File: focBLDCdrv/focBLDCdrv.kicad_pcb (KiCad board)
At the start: 2 copper layers, 78.5 x 50 mm, 19 parts, among them J1 Screw_Terminal_01x02, J2 Screw_Terminal_01x03, J5 Conn_02x03_Counter_Clockwise, J6 Conn_01x03, U1 MFC8316A

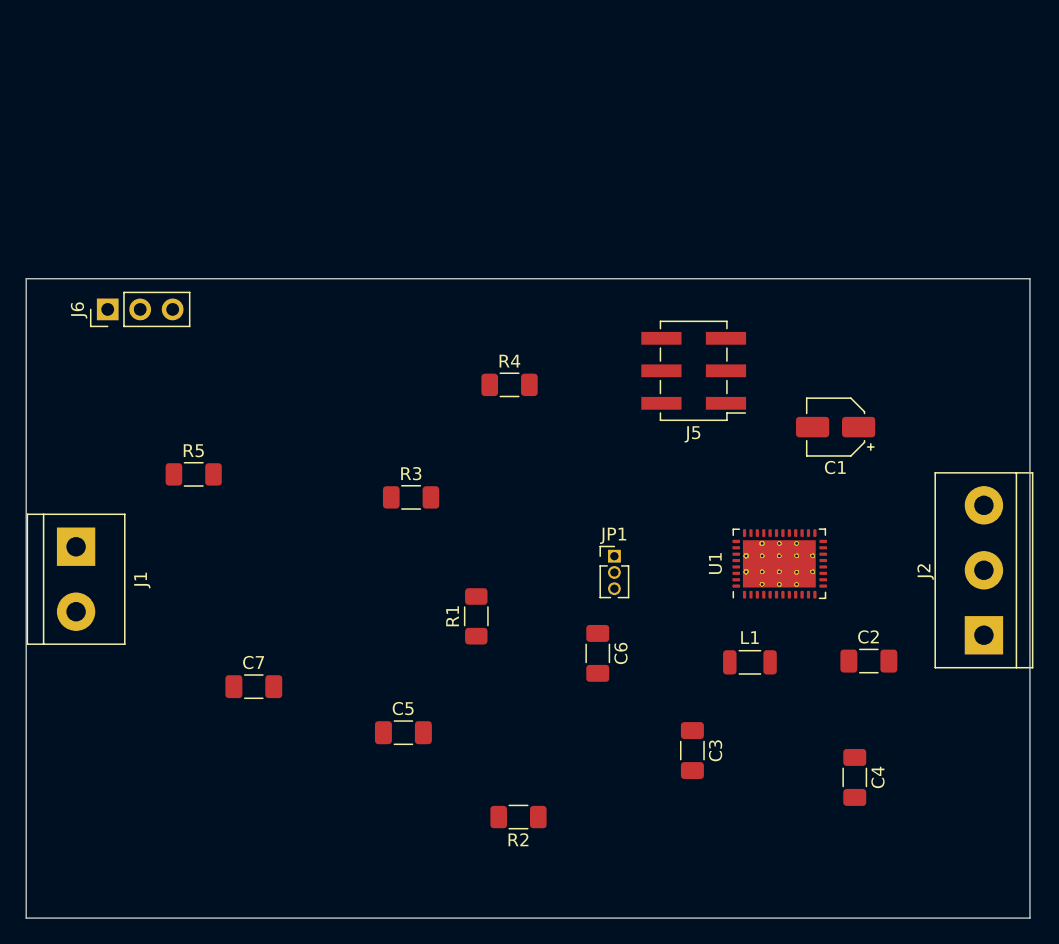
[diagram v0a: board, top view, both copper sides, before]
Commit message: J4 header orientation changed, mount holes added and additinal AGND fill
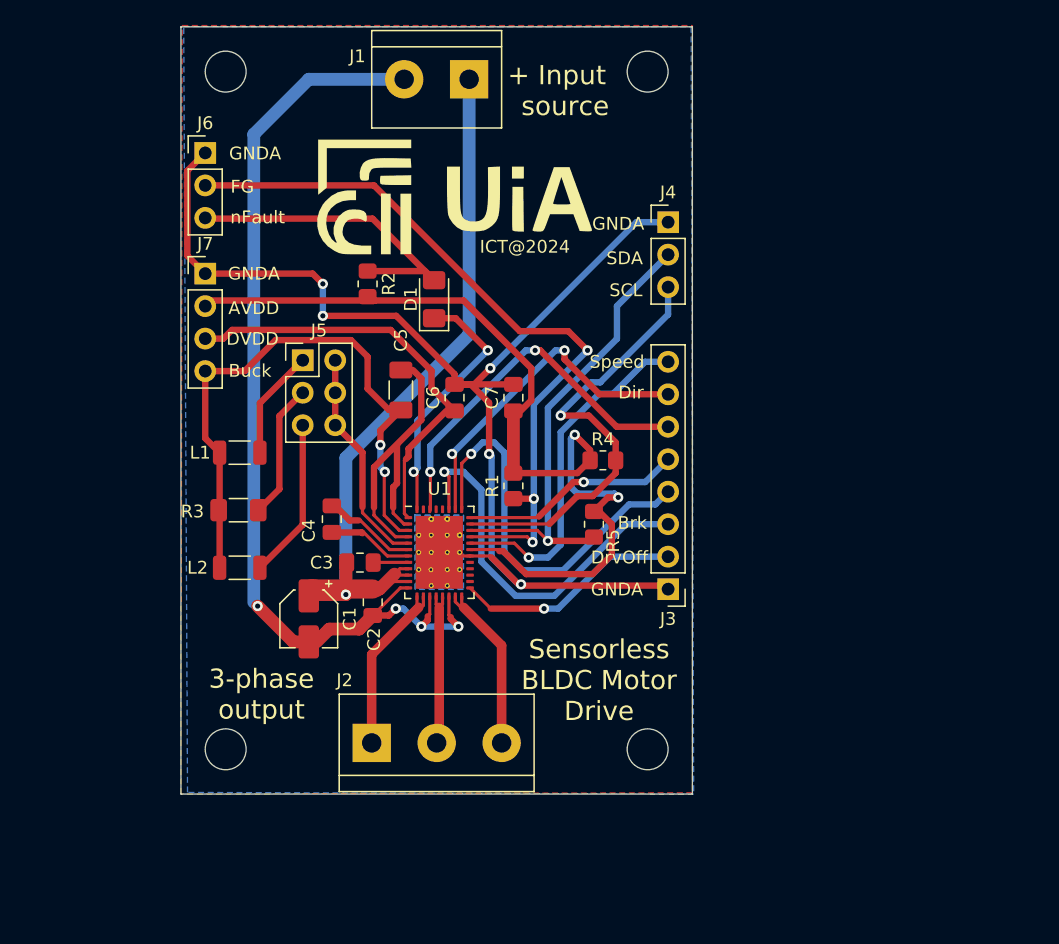
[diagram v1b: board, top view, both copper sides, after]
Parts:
- removed JP1: Jumper_3_Open, Connector_PinHeader_1.27mm:PinHeader_1x03_P1.27mm_Vertical
- added D1: LED, LED_SMD:LED_1206_3216Metric_Pad1.42x1.75mm_HandSolder, F.Cu at (147.9, 88.0)
- added G***: LOGO, UiA-Logo:uiaLogo, F.Cu at (149.5, 80.0)
- added J3: Conn_01x08, Connector_PinHeader_2.54mm:PinHeader_1x08_P2.54mm_Vertical, F.Cu at (166.2, 110.7)
- added J4: i2c, Connector_PinHeader_2.54mm:PinHeader_1x03_P2.54mm_Vertical, F.Cu at (166.2, 82.0)
- added J7: Power Out, Connector_PinHeader_2.54mm:PinHeader_1x04_P2.54mm_Vertical, F.Cu at (130.0, 86.0)
- added L2: 22µ, Inductor_SMD:L_1206_3216Metric, F.Cu at (132.7, 109.0)
- added REF**: MountingHole_3.2mm_M3, MountingHole:MountingHole_3.2mm_M3, F.Cu at (131.6, 70.2)
- added REF**: MountingHole_3.2mm_M3, MountingHole:MountingHole_3.2mm_M3, F.Cu at (164.6, 70.2)
- added REF**: MountingHole_3.2mm_M3, MountingHole:MountingHole_3.2mm_M3, F.Cu at (131.6, 123.2)
- added REF**: MountingHole_3.2mm_M3, MountingHole:MountingHole_3.2mm_M3, F.Cu at (164.6, 123.2)
- C2, C3, C4, C6, C7: footprint Capacitor_SMD:C_1206_3216Metric_Pad1.33x1.80mm_HandSolder -> Capacitor_SMD:C_0805_2012Metric_Pad1.18x1.45mm_HandSolder
- J5: value Conn_02x03_Counter_Clockwise -> Conn_02x03_Top_Bottom; footprint Connector_PinHeader_2.54mm:PinHeader_2x03_P2.54mm_Vertical_SMD -> Connector_PinHeader_2.54mm:PinHeader_2x03_P2.54mm_Vertical
- J6: value Conn_01x03 -> Monitor port
- R1: value 22 -> 4.7k; footprint Resistor_SMD:R_1206_3216Metric_Pad1.30x1.75mm_HandSolder -> Resistor_SMD:R_0805_2012Metric_Pad1.20x1.40mm_HandSolder
- R2: value 5.1k -> 1k; footprint Resistor_SMD:R_1206_3216Metric_Pad1.30x1.75mm_HandSolder -> Resistor_SMD:R_0805_2012Metric_Pad1.20x1.40mm_HandSolder
- R3: value 5.1k -> 22
- R4, R5: value 5.1k -> 4.7k; footprint Resistor_SMD:R_1206_3216Metric_Pad1.30x1.75mm_HandSolder -> Resistor_SMD:R_0805_2012Metric_Pad1.20x1.40mm_HandSolder
- moved J2 48.6 mm to (143.0, 122.7), turned to 0 degrees
- moved J1 47.8 mm to (150.6, 70.8), turned to 180 degrees
- moved C4 45.6 mm to (139.9, 105.2), turned to 90 degrees
- moved C1 43.8 mm to (138.1, 113.0), turned to -90 degrees
- moved R2 43.3 mm to (142.7, 86.8), turned to -90 degrees
- moved L1 43.1 mm to (132.7, 100.0)
- moved C2 39.1 mm to (143.1, 111.7), turned to -90 degrees
- moved R5 31.5 mm to (160.4, 105.6), turned to -90 degrees
- moved J5 30.6 mm to (137.6, 92.8), turned to 0 degrees
- moved C7 30.4 mm to (154.1, 95.7), turned to 90 degrees
- moved C3 29.9 mm to (142.1, 108.6), turned to 180 degrees
- moved C5 26.8 mm to (145.3, 95.1), turned to -90 degrees
- moved U1 26.6 mm to (148.3, 107.8), turned to 0 degrees
- moved C6 22.9 mm to (149.5, 95.7), turned to 90 degrees
- moved J6 14.4 mm to (130.0, 76.6), turned to 0 degrees
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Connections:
- net VDD renamed VM
- C1 pad 2: GND -> PNGD
- C2 pad 2: GND -> PNGD
- C5 pad 1: GND -> DGND
- C6 pad 2: GND -> GNDA
- C7 pad 1: GND -> AVDD
- C7 pad 2: GND -> GNDA
- J1 pad 2: GND -> PNGD
- J5 pad 1: SOX -> Net-(J5-Pad1)
- J5 pad 2: DIR -> Net-(J5-Pad2)
- J5 pad 3: DRVOFF -> Net-(J5-Pad3)
- J5 pad 4: EXT_CLK -> Net-(J5-Pad2)
- J5 pad 5: EXT_WD -> Net-(J5-Pad5)
- J5 pad 6: BRAKE -> Net-(J5-Pad2)
- J6 pad 1: nFAULT -> GNDA
- J6 pad 3: GND -> nFAULT
- L1 pad 2: Net-(L1-Pad2) -> Net-(J5-Pad1)
- R1 pad 1: BUCK -> FG
- R1 pad 2: Net-(R1-Pad2) -> AVDD
- R2 pad 2: GND -> AVDD
- R3 pad 1: FG -> BUCK
- R3 pad 2: AVDD -> Net-(J5-Pad3)
- R4 pad 1: GND -> AVDD
- R5 pad 1: GND -> AVDD
- U1 pad 12: GND -> PNGD
- U1 pad 15: GND -> PNGD
- U1 pad 18: GND -> PNGD
- U1 pad 2: GND -> DGND
- U1 pad 26: GND -> GNDA
- U1 pad 4: GND -> DGND
- U1 pad 40: nFAULT -> Net-(D1-Pad1)
- U1 pad 41: (no net) -> GNDA
- U1 pad 5: Net-(U1-Pad5) -> Net-(J5-Pad2)
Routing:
- net GNDA: track 0.00 -> 98.7 mm, vias 0 -> 5
- net PNGD: track 0.00 -> 78.1 mm, vias 0 -> 4
- net AVDD: track 0.00 -> 74.2 mm, vias 0 -> 2
- net VM: track 0.00 -> 62.6 mm, vias 0 -> 1
- net FG: track 0.00 -> 58.7 mm, vias 0 -> 3
- net BUCK: track 0.00 -> 47.4 mm, vias 0 -> 2
- net SDA: track 0.00 -> 36.4 mm, vias 0 -> 1
- net SCL: track 0.00 -> 34.5 mm, vias 0 -> 1
- net DVDD: track 0.00 -> 33.7 mm
- net EXT_CLK: track 0.00 -> 31.7 mm, vias 0 -> 1
- net BRAKE: track 0.00 -> 30.2 mm, vias 0 -> 1
- net SOX: track 0.00 -> 29.2 mm, vias 0 -> 2
- net SPEED: track 0.00 -> 27.4 mm, vias 0 -> 1
- net DIR: track 0.00 -> 26.5 mm, vias 0 -> 2
- net nFAULT: track 0.00 -> 25.4 mm
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- added copper zone on B.Cu, net GNDA
- added copper zone on F.Cu, net GNDA
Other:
- board size 78.5 x 50 mm -> 40 x 60 mm
- board text added: "+ Input source"
- board text added: "3-phase output"
- board text added: "AVDD"
- board text added: "Brk"
- board text added: "Buck"
- board text added: "DVDD"
- board text added: "Dir"
- board text added: "DrvOff"
- board text added: "FG"
- board text added: "GNDA"
- board text added: "ICT@2024"
- board text added: "SCL"
- board text added: "SDA"
- board text added: "Sensorless BLDC Motor Drive"
- board text added: "Speed"
- board text added: "nFault"
